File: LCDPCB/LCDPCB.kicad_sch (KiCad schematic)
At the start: 23 parts, among them J1 Sockets, J2 Hot plug, J3 Programming Header, SW1 SW_Push, U1 STM32F091RCT6, U2 LD1117S12TR_SOT223

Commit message: stuff
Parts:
- R4: footprint Resistor_SMD:R_0402_1005Metric -> lib_file:5.1kR
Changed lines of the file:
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@@
       (effects (font (size 1.27 1.27)) (justify left))
     )
-    (property "Footprint" "Resistor_SMD:R_0402_1005Metric" (id 2) (at 56.642 48.26 90)
+    (property "Footprint" "lib_file:5.1kR" (id 2) (at 56.642 48.26 90)
       (effects (font (size 1.27 1.27)) hide)
     )
@@
     )
     (path "/8efa2d6b-ac93-463d-8fc3-82bea1d9a16b"
-      (reference "R4") (unit 1) (value "5.1K") (footprint "Resistor_SMD:R_0402_1005Metric")
+      (reference "R4") (unit 1) (value "5.1K") (footprint "lib_file:5.1kR")
     )
     (path "/763fa959-745c-4cb0-8869-5f2c5ac68c34"

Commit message: added pcb for lcd
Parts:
- D2, D3: footprint lib_file:BAT60B -> lib_file:BAT60JFILM
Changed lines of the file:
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@@
     (property "Reference" "D3" (id 0) (at 44.7675 38.1 0))
     (property "Value" "BAT60A" (id 1) (at 44.7675 40.64 0))
-    (property "Footprint" "lib_file:BAT60B" (id 2) (at 44.45 40.005 0)
+    (property "Footprint" "lib_file:BAT60JFILM" (id 2) (at 44.45 40.005 0)
       (effects (font (size 1.27 1.27)) hide)
     )
@@
     (property "Reference" "D2" (id 0) (at 73.9775 68.58 0))
     (property "Value" "BAT60A" (id 1) (at 73.9775 71.12 0))
-    (property "Footprint" "lib_file:BAT60B" (id 2) (at 73.66 70.485 0)
+    (property "Footprint" "lib_file:BAT60JFILM" (id 2) (at 73.66 70.485 0)
       (effects (font (size 1.27 1.27)) hide)
     )
@@
     )
     (path "/f3eeaca9-01b9-45ab-a60b-99a2befb5b1d"
-      (reference "D2") (unit 1) (value "BAT60A") (footprint "lib_file:BAT60B")
+      (reference "D2") (unit 1) (value "BAT60A") (footprint "lib_file:BAT60JFILM")
     )
     (path "/eb4cb8d8-0281-4c02-b2b5-842a27215625"
-      (reference "D3") (unit 1) (value "BAT60A") (footprint "lib_file:BAT60B")
+      (reference "D3") (unit 1) (value "BAT60A") (footprint "lib_file:BAT60JFILM")
     )
     (path "/bf39286c-c998-45e7-99b6-5106f72f3fcc"

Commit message: stuff
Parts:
- U2: footprint lib_file:LD1117 -> Package_TO_SOT_SMD:SOT-223-3_TabPin2
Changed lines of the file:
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@@
     (pin "2")
-  )
-  (symbol (lib_id "Regulator_Linear:LD1117S12TR_SOT223") (at 48.26 74.93 0) (unit 1)
-    (in_bom yes) (on_board yes) (fields_autoplaced)
-    (property "Reference" "U2" (id 0) (at 48.26 67.31 0))
-    (property "Value" "LD1117S12TR_SOT223" (id 1) (at 48.26 69.85 0))
-    (property "Footprint" "lib_file:LD1117" (id 2) (at 48.26 69.85 0)
-      (effects (font (size 1.27 1.27)) hide)
-    )
-    (property "Datasheet" "http://www.st.com/st-web-ui/static/active/en/resource/technical/document/datasheet/CD00000544.pdf" (id 3) (at 50.8 81.28 0)
-      (effects (font (size 1.27 1.27)) hide)
-    )
-    (pin "1")
-    (pin "2")
-    (pin "3")
   )
   (symbol (lib_id "power:+3V0") (at 231.14 104.14 0) (unit 1)
@@
     (pin "2")
   )
+  (symbol (lib_id "Regulator_Linear:LD1117S12TR_SOT223") (at 48.26 74.93 0) (unit 1)
+    (in_bom yes) (on_board yes) (fields_autoplaced)
+    (property "Reference" "U2" (id 0) (at 48.26 67.31 0))
+    (property "Value" "LD1117S12TR_SOT223" (id 1) (at 48.26 69.85 0))
+    (property "Footprint" "Package_TO_SOT_SMD:SOT-223-3_TabPin2" (id 2) (at 48.26 69.85 0)
+      (effects (font (size 1.27 1.27)) hide)
+    )
+    (property "Datasheet" "http://www.st.com/st-web-ui/static/active/en/resource/technical/document/datasheet/CD00000544.pdf" (id 3) (at 50.8 81.28 0)
+      (effects (font (size 1.27 1.27)) hide)
+    )
+    (pin "1")
+    (pin "2")
+    (pin "3")
+  )
   (sheet_instances
     (path "/" (page "1"))
@@
       (reference "U1") (unit 1) (value "STM32F091RCT6") (footprint "lib_file:STM32F091")
     )
-    (path "/347a6986-567c-41a0-b68f-23cd921c3c50"
-      (reference "U2") (unit 1) (value "LD1117S12TR_SOT223") (footprint "lib_file:LD1117")
-    )
-  )
+    (path "/fbc67559-7a68-4877-8113-d2e897e12db4"
+      (reference "U2") (unit 1) (value "LD1117S12TR_SOT223") (footprint "Package_TO_SOT_SMD:SOT-223-3_TabPin2")
+    )
+  )

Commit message: added midterm review
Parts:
- D2: value BAT60A -> BAT60JFLIM
- D3: value BAT60A -> BAT60JFILM
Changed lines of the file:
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@@
     (in_bom yes) (on_board yes) (fields_autoplaced)
     (property "Reference" "D3" (id 0) (at 44.7675 38.1 0))
-    (property "Value" "BAT60A" (id 1) (at 44.7675 40.64 0))
+    (property "Value" "BAT60JFILM" (id 1) (at 44.7675 40.64 0))
     (property "Footprint" "lib_file:BAT60JFILM" (id 2) (at 44.45 40.005 0)
       (effects (font (size 1.27 1.27)) hide)
@@
     (in_bom yes) (on_board yes) (fields_autoplaced)
     (property "Reference" "D2" (id 0) (at 73.9775 68.58 0))
-    (property "Value" "BAT60A" (id 1) (at 73.9775 71.12 0))
+    (property "Value" "BAT60JFLIM" (id 1) (at 73.9775 71.12 0))
     (property "Footprint" "lib_file:BAT60JFILM" (id 2) (at 73.66 70.485 0)
       (effects (font (size 1.27 1.27)) hide)
@@
     )
     (path "/f3eeaca9-01b9-45ab-a60b-99a2befb5b1d"
-      (reference "D2") (unit 1) (value "BAT60A") (footprint "lib_file:BAT60JFILM")
+      (reference "D2") (unit 1) (value "BAT60JFLIM") (footprint "lib_file:BAT60JFILM")
     )
     (path "/eb4cb8d8-0281-4c02-b2b5-842a27215625"
-      (reference "D3") (unit 1) (value "BAT60A") (footprint "lib_file:BAT60JFILM")
+      (reference "D3") (unit 1) (value "BAT60JFILM") (footprint "lib_file:BAT60JFILM")
     )
     (path "/bf39286c-c998-45e7-99b6-5106f72f3fcc"

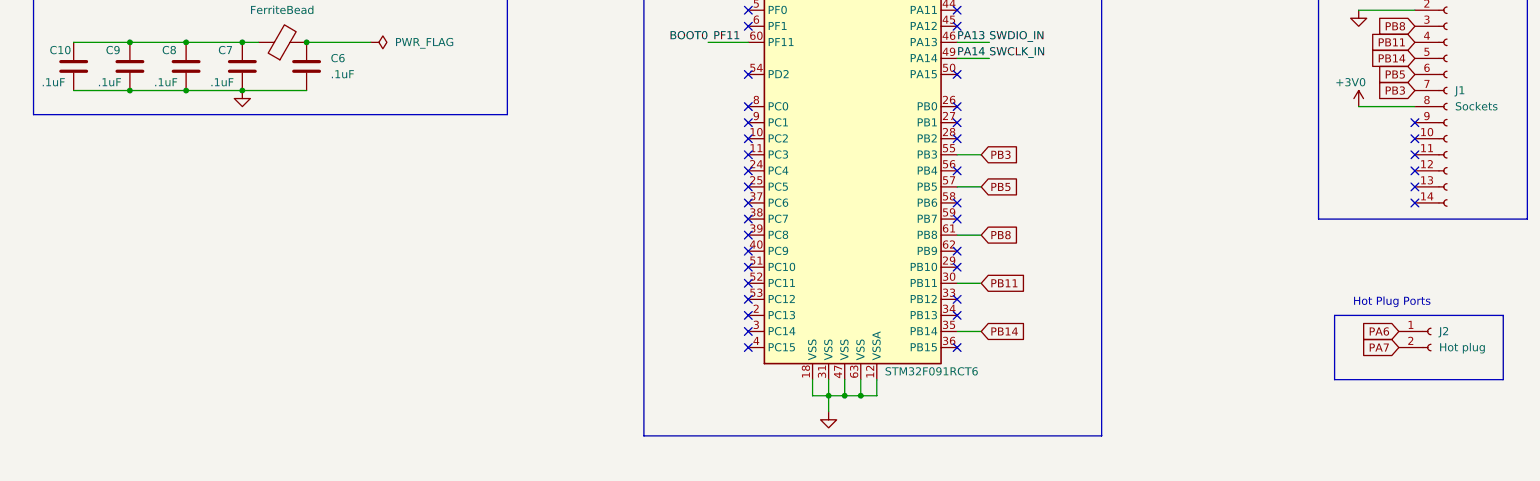
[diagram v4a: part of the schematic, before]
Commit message: updated with pins
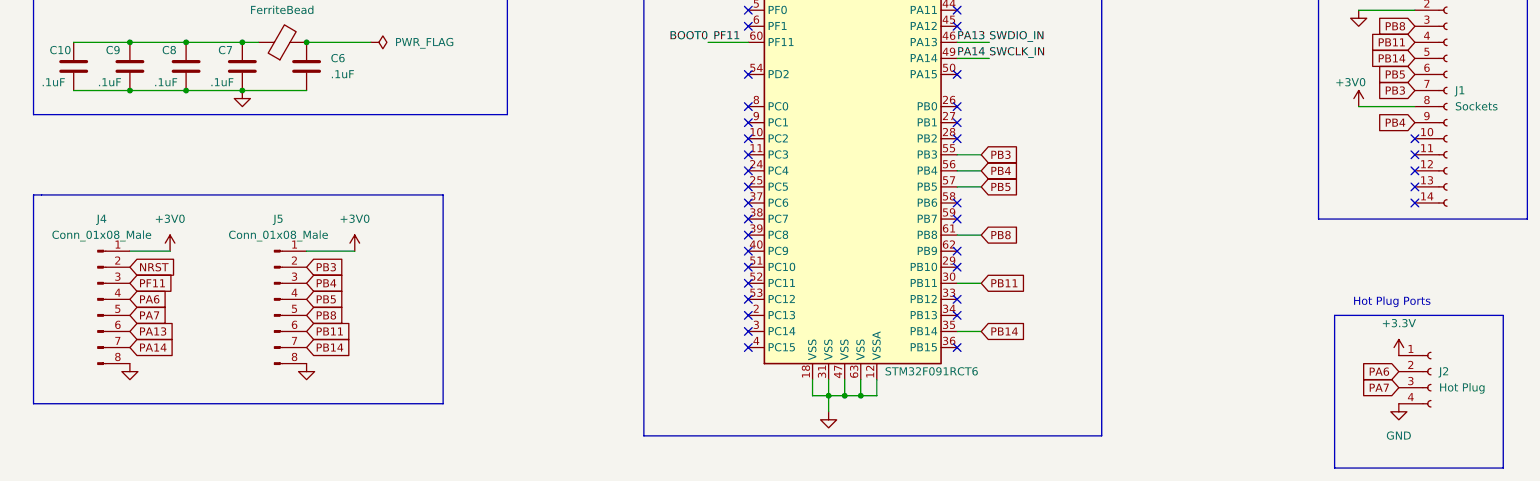
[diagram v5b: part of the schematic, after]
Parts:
- removed J2: Hot plug, Connector_PinSocket_2.54mm:PinSocket_1x02_P2.54mm_Vertical, symbol Connector:Conn_01x02_Female
- added J2: Hot Plug, Connector_PinSocket_2.54mm:PinSocket_1x04_P2.54mm_Vertical, symbol Connector:Conn_01x04_Female
- added J4, J5: Conn_01x08_Male, Connector_PinHeader_2.54mm:PinHeader_1x08_P2.54mm_Vertical, symbol Connector:Conn_01x08_Male
- SW1: footprint Button_Switch_THT:SW_PUSH-12mm -> lib_file:Button
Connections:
- net +3V0: now also J4.1 (Pin_1), J5.1 (Pin_1)
- net GND: now also J2.4 (Pin_4), J4.8 (Pin_8), J5.8 (Pin_8)
- net NRST: now also J4.2 (Pin_2)
- net PA13: now also J4.6 (Pin_6)
- net PA14: now also J4.7 (Pin_7)
- net PA6: now also J2.2 (Pin_2), J4.4 (Pin_4)
- net PA7: now also J2.3 (Pin_3), J4.5 (Pin_5)
- net PB11: now also J5.6 (Pin_6)
- net PB14: now also J5.7 (Pin_7)
- net PB3: now also J5.2 (Pin_2)
- net PB5: now also J5.4 (Pin_4)
- net PB8: now also J5.5 (Pin_5)
- net PB4: now reaches U1.56 (PB4)
- net PB4: now also J1.9 (Pin_9), J5.3 (Pin_3)
- net BOOT0 renamed PF11
- net PF11: now also J4.3 (Pin_3)
- new net +3.3V: J2.1 (Pin_1)
- no-connect marks 49 -> 47

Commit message: display done
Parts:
- added H1, H2, H3, H4: MountingHole, MountingHole:MountingHole_2.2mm_M2_ISO7380, symbol Mechanical:MountingHole
- C1, C10, C3, C4, C6, C7, C8, C9: footprint lib_file:.1uFC -> lib_file:CAPC3225X88N
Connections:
- net +3V0: now also C10.1, C7.1, C8.1, C9.1, FB1.1
- net +5V: now also C2.1, C3.1, U2.3 (VI)
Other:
- note added: "Connectors for Testing"
- note added: "Mounting Holes"

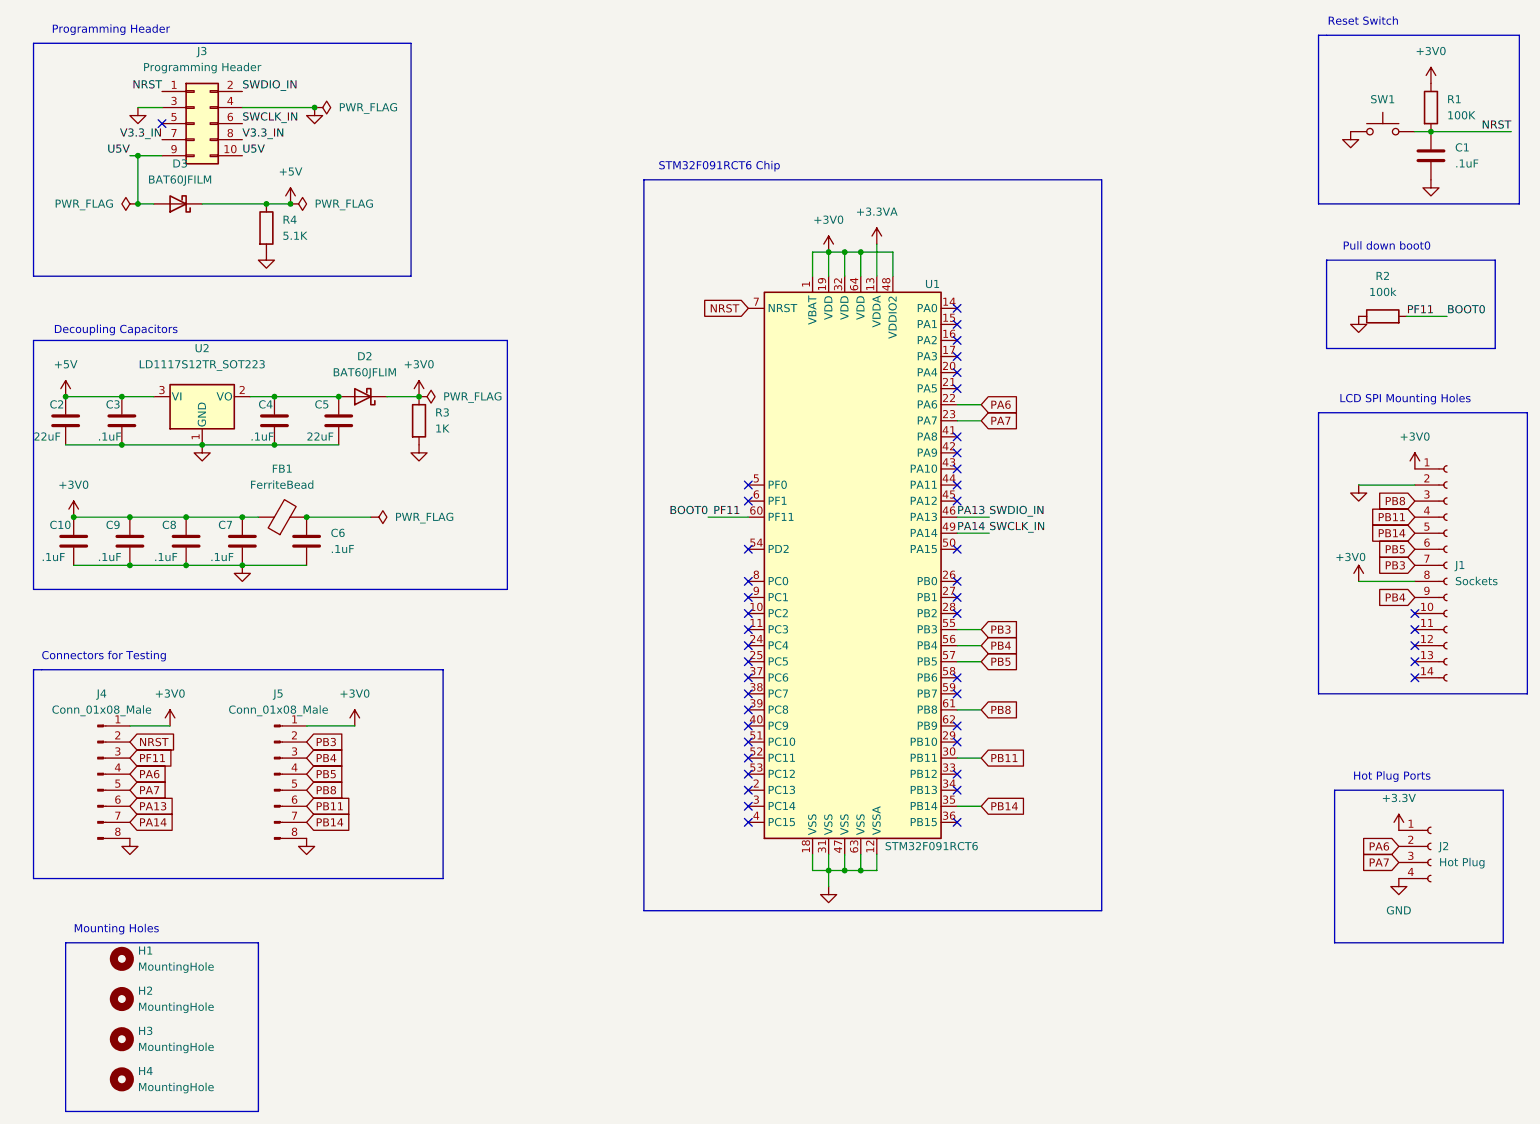
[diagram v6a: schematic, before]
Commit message: fixed 1kR
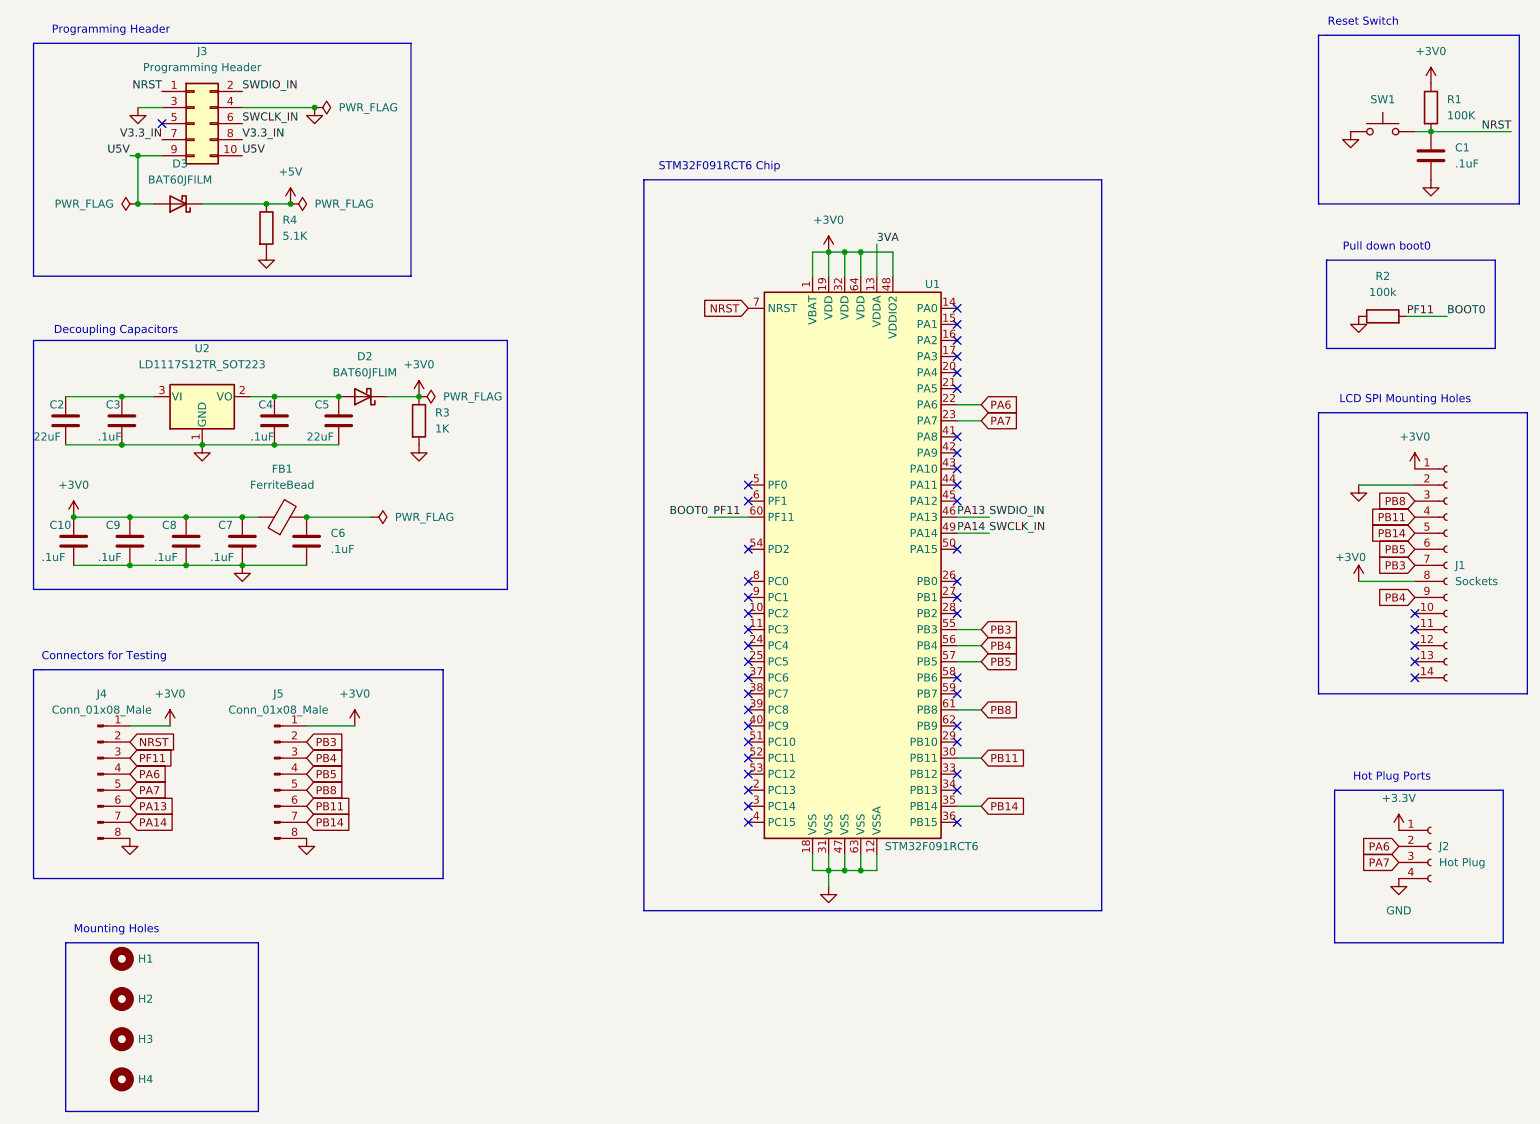
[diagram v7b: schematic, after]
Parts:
- R3: footprint lib_file:1kR -> lib_file:ERJUP3
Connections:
- net +5V: no longer C2.1, C3.1, U2.3 (VI)
- net +3.3VA renamed 3VA
- new net: C2.1, C3.1, U2.3 (VI)
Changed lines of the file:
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@@
   (junction (at 69.85 74.93) (diameter 0) (color 0 0 0 0)
-  )
-  (junction (at 26.67 74.93) (diameter 0) (color 0 0 0 0)
   )
   (junction (at 36.83 101.6) (diameter 0) (color 0 0 0 0)
@@
     (effects (font (size 1.27 1.27)) (justify right bottom))
   )
+  (label "3VA" (at 154.94 50.8 0)
+    (effects (font (size 1.27 1.27)) (justify left bottom))
+  )
   (label "V3.3_IN" (at 41.91 34.29 180)
     (effects (font (size 1.27 1.27)) (justify right bottom))
@@
     (pin "1")
   )
-  (symbol (lib_id "power:+3.3VA") (at 154.94 50.8 0) (unit 1)
-    (in_bom yes) (on_board yes) (fields_autoplaced)
-    (property "Reference" "#PWR0101" (id 0) (at 154.94 54.61 0)
-      (effects (font (size 1.27 1.27)) hide)
-    )
-    (property "Value" "+3.3VA" (id 1) (at 154.94 45.72 0))
-    (property "Footprint" "" (id 2) (at 154.94 50.8 0)
-      (effects (font (size 1.27 1.27)) hide)
-    )
-    (property "Datasheet" "" (id 3) (at 154.94 50.8 0)
-      (effects (font (size 1.27 1.27)) hide)
-    )
-    (pin "1")
-  )
   (symbol (lib_id "Device:R") (at 82.55 78.74 0) (unit 1)
     (in_bom yes) (on_board yes) (fields_autoplaced)
@@
       (effects (font (size 1.27 1.27)) (justify left))
     )
-    (property "Footprint" "lib_file:1kR" (id 2) (at 80.772 78.74 90)
+    (property "Footprint" "lib_file:ERJUP3" (id 2) (at 80.772 78.74 90)
       (effects (font (size 1.27 1.27)) hide)
     )
@@
   (symbol (lib_id "Mechanical:MountingHole") (at 35.56 176.53 0) (unit 1)
     (in_bom yes) (on_board yes) (fields_autoplaced)
-    (property "Reference" "H3" (id 0) (at 38.1 175.2599 0)
+    (property "Reference" "H3" (id 0) (at 38.1 176.5299 0)
       (effects (font (size 1.27 1.27)) (justify left))
     )
     (property "Value" "MountingHole" (id 1) (at 38.1 177.7999 0)
-      (effects (font (size 1.27 1.27)) (justify left))
+      (effects (font (size 1.27 1.27)) (justify left) hide)
     )
     (property "Footprint" "MountingHole:MountingHole_2.2mm_M2_ISO7380" (id 2) (at 35.56 176.53 0)
@@
   (symbol (lib_id "Mechanical:MountingHole") (at 35.56 170.18 0) (unit 1)
     (in_bom yes) (on_board yes) (fields_autoplaced)
-    (property "Reference" "H2" (id 0) (at 38.1 168.9099 0)
+    (property "Reference" "H2" (id 0) (at 38.1 170.1799 0)
       (effects (font (size 1.27 1.27)) (justify left))
     )
     (property "Value" "MountingHole" (id 1) (at 38.1 171.4499 0)
-      (effects (font (size 1.27 1.27)) (justify left))
+      (effects (font (size 1.27 1.27)) (justify left) hide)
     )
     (property "Footprint" "MountingHole:MountingHole_2.2mm_M2_ISO7380" (id 2) (at 35.56 170.18 0)
@@
   (symbol (lib_id "Mechanical:MountingHole") (at 35.56 182.88 0) (unit 1)
     (in_bom yes) (on_board yes) (fields_autoplaced)
-    (property "Reference" "H4" (id 0) (at 38.1 181.6099 0)
+    (property "Reference" "H4" (id 0) (at 38.1 182.8799 0)
       (effects (font (size 1.27 1.27)) (justify left))
     )
     (property "Value" "MountingHole" (id 1) (at 38.1 184.1499 0)
-      (effects (font (size 1.27 1.27)) (justify left))
+      (effects (font (size 1.27 1.27)) (justify left) hide)
     )
     (property "Footprint" "MountingHole:MountingHole_2.2mm_M2_ISO7380" (id 2) (at 35.56 182.88 0)
@@
   (symbol (lib_id "Mechanical:MountingHole") (at 35.56 163.83 0) (unit 1)
     (in_bom yes) (on_board yes) (fields_autoplaced)
-    (property "Reference" "H1" (id 0) (at 38.1 162.5599 0)
+    (property "Reference" "H1" (id 0) (at 38.1 163.8299 0)
       (effects (font (size 1.27 1.27)) (justify left))
     )
     (property "Value" "MountingHole" (id 1) (at 38.1 165.0999 0)
-      (effects (font (size 1.27 1.27)) (justify left))
+      (effects (font (size 1.27 1.27)) (justify left) hide)
     )
     (property "Footprint" "MountingHole:MountingHole_2.2mm_M2_ISO7380" (id 2) (at 35.56 163.83 0)
@@
     (pin "2")
   )
-  (symbol (lib_id "power:+5V") (at 26.67 74.93 0) (unit 1)
-    (in_bom yes) (on_board yes) (fields_autoplaced)
-    (property "Reference" "#PWR?" (id 0) (at 26.67 78.74 0)
-      (effects (font (size 1.27 1.27)) hide)
-    )
-    (property "Value" "+5V" (id 1) (at 26.67 69.85 0))
-    (property "Footprint" "" (id 2) (at 26.67 74.93 0)
-      (effects (font (size 1.27 1.27)) hide)
-    )
-    (property "Datasheet" "" (id 3) (at 26.67 74.93 0)
-      (effects (font (size 1.27 1.27)) hide)
-    )
-    (pin "1")
-  )
   (symbol (lib_id "power:GND") (at 66.04 29.21 0) (unit 1)
     (in_bom yes) (on_board yes) (fields_autoplaced)
@@
       (reference "#FLG0105") (unit 1) (value "PWR_FLAG") (footprint "")
     )
-    (path "/141b3fd1-0e42-4a0b-bcb0-9e9234e702c6"
-      (reference "#PWR0101") (unit 1) (value "+3.3VA") (footprint "")
-    )
     (path "/074a7861-abd0-4f08-8396-c8f3be25f6d3"
       (reference "#PWR0102") (unit 1) (value "+3.3V") (footprint "")
@@
       (reference "#PWR0125") (unit 1) (value "GND") (footprint "")
     )
-    (path "/edcfd4ad-e191-42c3-8c4e-09f5341839ff"
-      (reference "#PWR?") (unit 1) (value "+5V") (footprint "")
-    )
     (path "/288a3ec0-122f-4360-968a-e07818d05bc7"
       (reference "C1") (unit 1) (value ".1uF") (footprint "lib_file:CAPC3225X88N")
@@
     )
     (path "/1b63d79f-2851-4bcf-b622-bb66c0b5c1ae"
-      (reference "R3") (unit 1) (value "1K") (footprint "lib_file:1kR")
+      (reference "R3") (unit 1) (value "1K") (footprint "lib_file:ERJUP3")
     )
     (path "/8efa2d6b-ac93-463d-8fc3-82bea1d9a16b"
